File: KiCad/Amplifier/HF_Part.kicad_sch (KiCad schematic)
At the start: 11 parts, among them U3 BLF188XRU

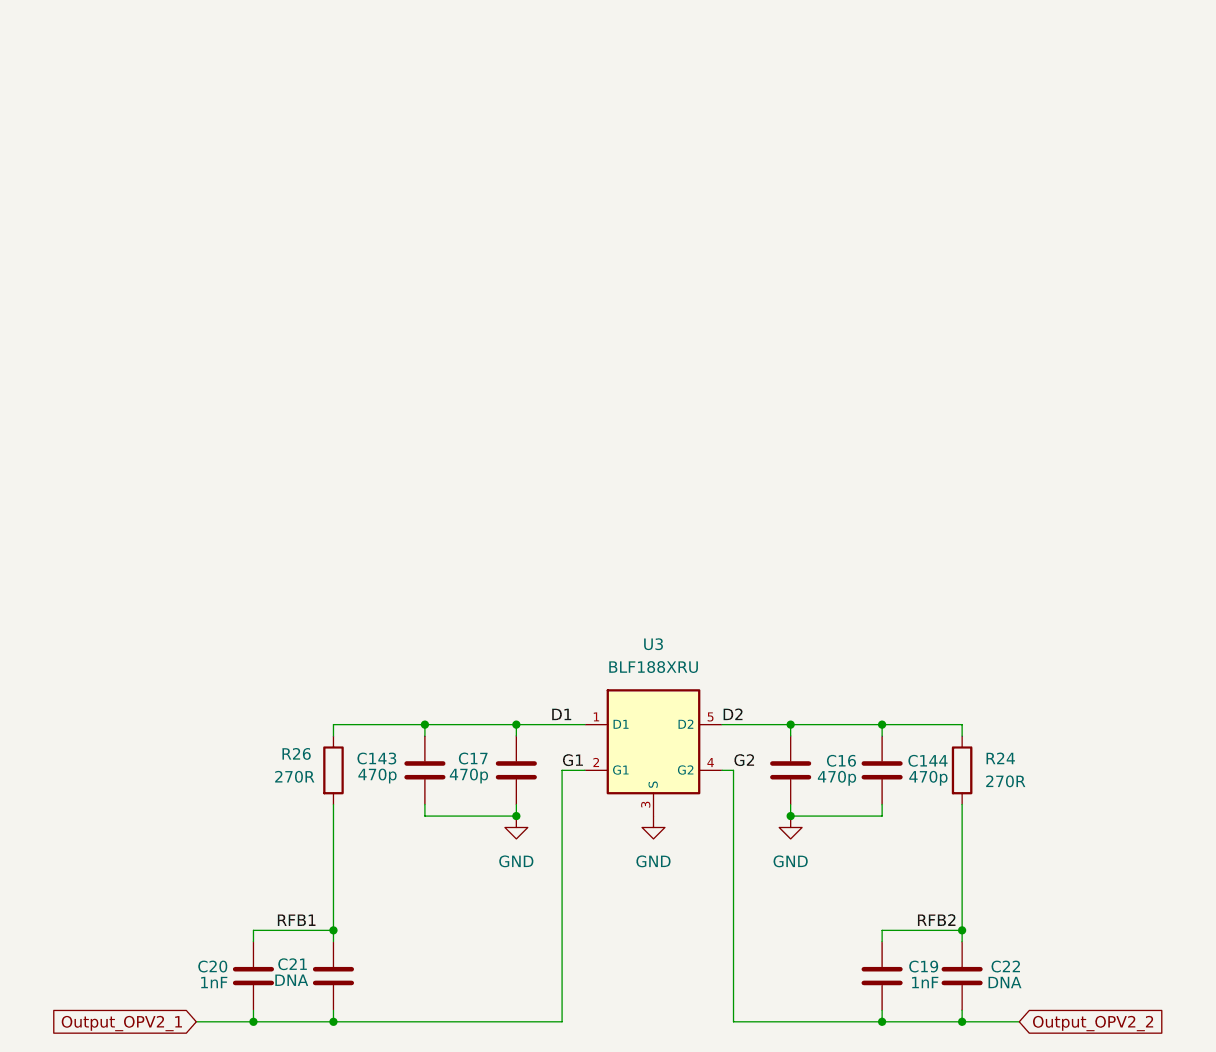
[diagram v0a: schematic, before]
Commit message: Platinenentwurf
die Platine wurde aufgebaut. Kontrolle fehlt
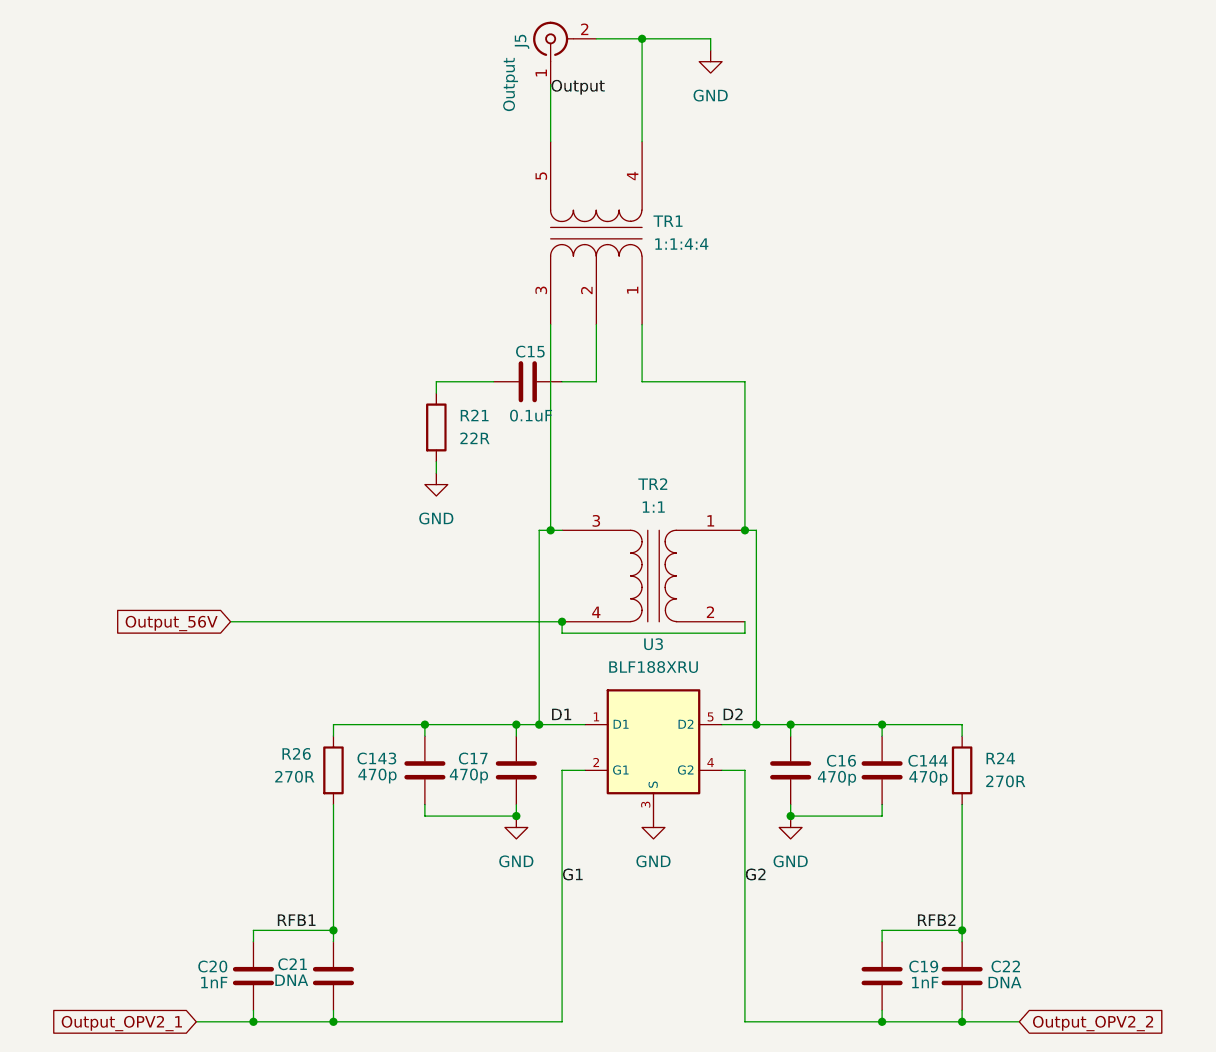
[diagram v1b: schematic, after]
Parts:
- added C15: 0.1uF, Capacitor_SMD:C_0603_1608Metric_Pad1.08x0.95mm_HandSolder, symbol Device:C
- added J5: Output, Connector_Coaxial:SMA_Amphenol_901-144_Vertical, symbol Connector:Conn_Coaxial
- added R21: 22R, Resistor_SMD:R_0603_1608Metric_Pad0.98x0.95mm_HandSolder, symbol Device:R
- added TR1: 1:1:4:4, Library:TR1, symbol Device:Transformer_SP_1S
- added TR2: 1:1, Library:TR2, symbol Device:Transformer_1P_1S
- C143, C144, C16, C17: footprint Capacitor_SMD:C_0603_1608Metric_Pad1.08x0.95mm_HandSolder -> Capacitor_SMD:C_1210_3225Metric_Pad1.33x2.70mm_HandSolder
- R24, R26: footprint Resistor_SMD:R_0603_1608Metric_Pad0.98x0.95mm_HandSolder -> Library:AX_1.000X.225_.034
- U3: footprint (none) -> Library:SOT539A
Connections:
- net D1: now also TR1.3 (PR1), TR2.3 (AA)
- net D2: now also TR1.1 (PR2), TR2.1 (SB)
- net GND: now also J5.2 (Ext), R21.2, TR1.4 (S1)
- new net: C15.1, R21.1
- new net: C15.2, TR1.2 (PM)
- new net Output: J5.1 (In), TR1.5 (S2)
- new net Output_56V: TR2.2 (SA), TR2.4 (AB)
